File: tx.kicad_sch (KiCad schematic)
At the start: 48 parts, among them J13 RFShield_Frame, J5 SWH, J7 SMA, T2 RF_BALUN, U12 MAX2831, U13 TXIF_BALUN, U16 DPDT

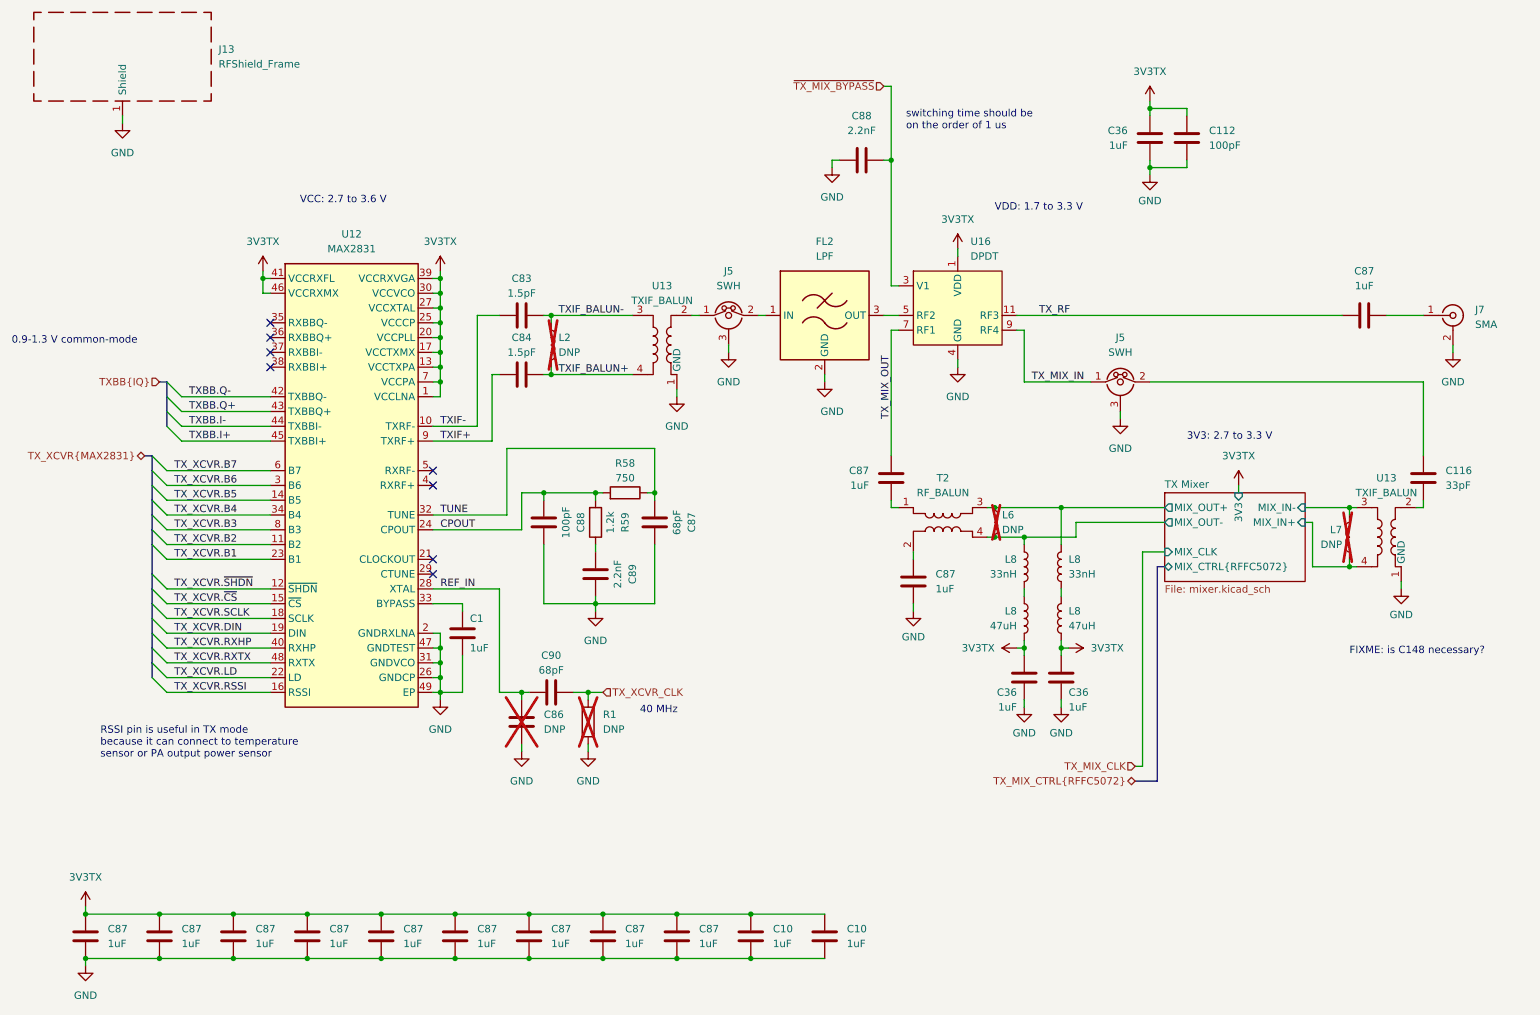
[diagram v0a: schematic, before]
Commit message: Replace open drain clock inverters with push-pull
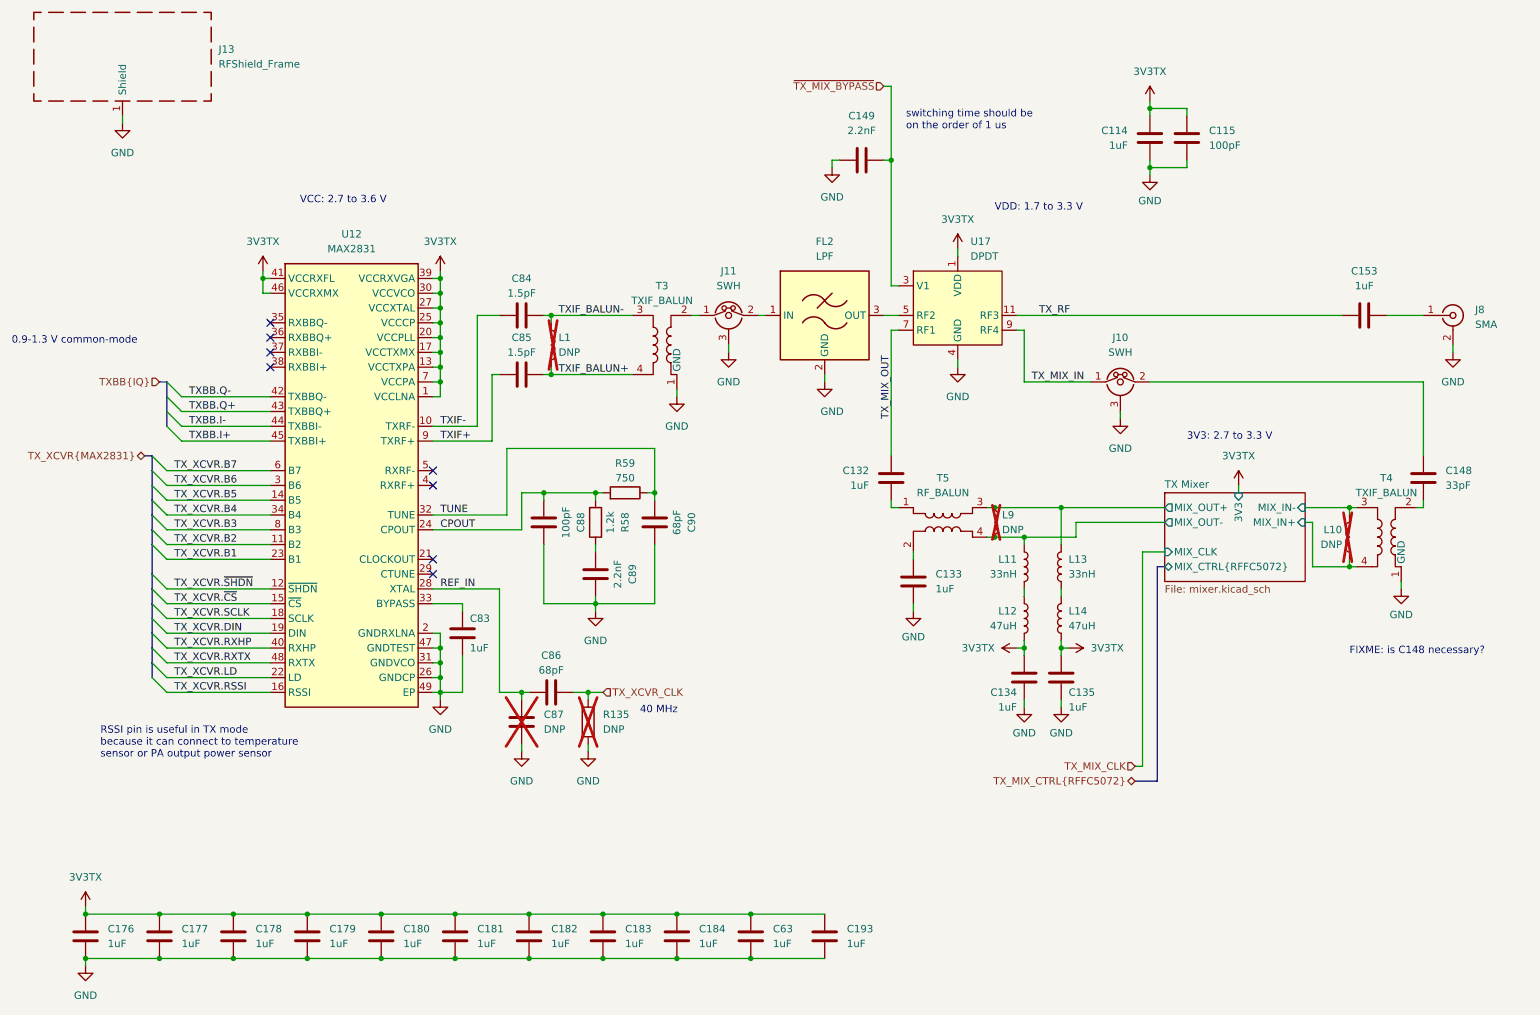
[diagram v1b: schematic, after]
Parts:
- renumbered C36 to C114, C112 to C115, C87 to C132, C87 to C133, C36 to C134, C36 to C135, C116 to C148, C88 to C149, C87 to C153, C87 to C176, C87 to C177, C87 to C178, C87 to C179, C87 to C180, C87 to C181, C87 to C182, C87 to C183, C87 to C184, C10 to C193, C10 to C63, C1 to C83, C83 to C84, C84 to C85, C90 to C86, C86 to C87, C87 to C90, J5 to J10, J5 to J11, J7 to J8, L2 to L1, L7 to L10, L8 to L11, L8 to L12, L8 to L13, L8 to L14, L6 to L9, R1 to R135, R59 to R58, R58 to R59, U13 to T3, U13 to T4, T2 to T5, U16 to U17

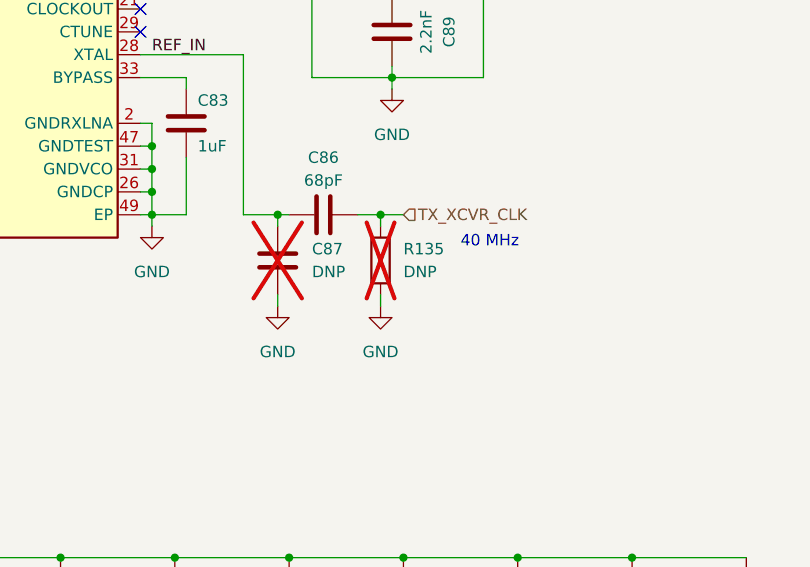
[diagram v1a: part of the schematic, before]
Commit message: Tune clock passives
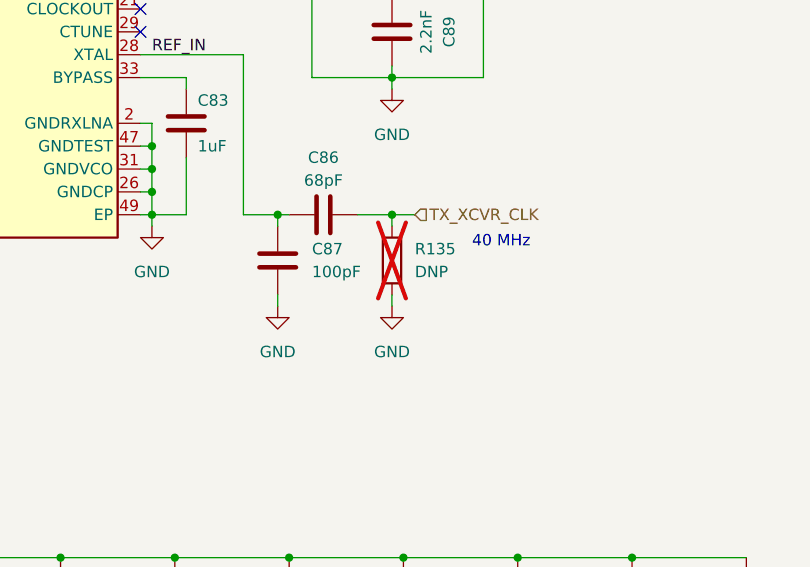
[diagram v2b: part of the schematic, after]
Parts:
- C87: value DNP -> 100pF; Manufacturer (none) -> Samsung; Part Number (none) -> CL03C101JA3NNNC; now fitted
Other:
- moved on the sheet: R135
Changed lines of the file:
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@@
   (junction (at 193.04 113.03) (diameter 0) (color 0 0 0 0)
   )
-  (junction (at 118.11 139.7) (diameter 0) (color 0 0 0 0)
+  (junction (at 119.38 139.7) (diameter 0) (color 0 0 0 0)
   )
   (junction (at 82.55 177.8) (diameter 0) (color 0 0 0 0)
@@
     (stroke (width 0) (type default))
   )
-  (wire (pts (xy 118.11 148.59) (xy 118.11 149.86))
+  (wire (pts (xy 119.38 148.59) (xy 119.38 149.86))
     (stroke (width 0) (type default))
   )
@@
     (stroke (width 0) (type default))
   )
-  (wire (pts (xy 118.11 139.7) (xy 120.65 139.7))
+  (wire (pts (xy 119.38 139.7) (xy 121.92 139.7))
     (stroke (width 0) (type default))
   )
@@
     (stroke (width 0) (type default))
   )
-  (wire (pts (xy 118.11 139.7) (xy 118.11 140.97))
+  (wire (pts (xy 119.38 139.7) (xy 119.38 140.97))
     (stroke (width 0) (type default))
   )
@@
     (stroke (width 0) (type default))
   )
-  (wire (pts (xy 115.57 139.7) (xy 118.11 139.7))
+  (wire (pts (xy 115.57 139.7) (xy 119.38 139.7))
     (stroke (width 0) (type default))
   )
@@
     (stroke (width 0) (type default))
   )
-  (text "40 MHz" (at 127 143.51 0)
+  (text "40 MHz" (at 128.27 143.51 0)
     (effects (font (size 1.27 1.27)) (justify left bottom))
   )
@@
     (effects (font (size 1.27 1.27)) (justify right))
   )
-  (hierarchical_label "TX_XCVR_CLK" (shape input) (at 120.65 139.7 0) (fields_autoplaced)
+  (hierarchical_label "TX_XCVR_CLK" (shape input) (at 121.92 139.7 0) (fields_autoplaced)
     (effects (font (size 1.27 1.27)) (justify left))
   )
@@
     )
   )
-  (symbol (lib_id "Device:R") (at 118.11 144.78 0) (unit 1)
+  (symbol (lib_id "Device:R") (at 119.38 144.78 0) (unit 1)
     (in_bom yes) (on_board yes) (dnp yes) (fields_autoplaced)
-    (property "Reference" "R135" (at 120.65 143.51 0)
+    (property "Reference" "R135" (at 121.92 143.51 0)
       (effects (font (size 1.27 1.27)) (justify left))
     )
-    (property "Value" "DNP" (at 120.65 146.05 0)
+    (property "Value" "DNP" (at 121.92 146.05 0)
       (effects (font (size 1.27 1.27)) (justify left))
     )
-    (property "Footprint" "Resistor_SMD:R_0402_1005Metric" (at 116.332 144.78 90)
-      (effects (font (size 1.27 1.27)) hide)
-    )
-    (property "Datasheet" "~" (at 118.11 144.78 0)
-      (effects (font (size 1.27 1.27)) hide)
-    )
-    (property "Part Number" "" (at 118.11 144.78 0)
-      (effects (font (size 1.27 1.27)) hide)
-    )
-    (property "Substitution" "" (at 118.11 144.78 0)
-      (effects (font (size 1.27 1.27)) hide)
-    )
-    (property "Description" "" (at 118.11 144.78 0)
-      (effects (font (size 1.27 1.27)) hide)
-    )
-    (property "Manufacturer" "" (at 118.11 144.78 0)
+    (property "Footprint" "Resistor_SMD:R_0402_1005Metric" (at 117.602 144.78 90)
+      (effects (font (size 1.27 1.27)) hide)
+    )
+    (property "Datasheet" "~" (at 119.38 144.78 0)
+      (effects (font (size 1.27 1.27)) hide)
+    )
+    (property "Part Number" "" (at 119.38 144.78 0)
+      (effects (font (size 1.27 1.27)) hide)
+    )
+    (property "Substitution" "" (at 119.38 144.78 0)
+      (effects (font (size 1.27 1.27)) hide)
+    )
+    (property "Description" "" (at 119.38 144.78 0)
+      (effects (font (size 1.27 1.27)) hide)
+    )
+    (property "Manufacturer" "" (at 119.38 144.78 0)
       (effects (font (size 1.27 1.27)) hide)
     )
@@
   )
   (symbol (lib_id "Device:C") (at 106.68 144.78 0) (unit 1)
-    (in_bom yes) (on_board yes) (dnp yes) (fields_autoplaced)
+    (in_bom yes) (on_board yes) (dnp no) (fields_autoplaced)
     (property "Reference" "C87" (at 110.49 143.51 0)
       (effects (font (size 1.27 1.27)) (justify left))
     )
-    (property "Value" "DNP" (at 110.49 146.05 0)
+    (property "Value" "100pF" (at 110.49 146.05 0)
       (effects (font (size 1.27 1.27)) (justify left))
     )
@@
       (effects (font (size 1.27 1.27)) hide)
     )
+    (property "Description" "CAP CER 100PF 25V C0G/NP0 0201" (at 106.68 144.78 0)
+      (effects (font (size 1.27 1.27)) hide)
+    )
+    (property "Manufacturer" "Samsung" (at 106.68 144.78 0)
+      (effects (font (size 1.27 1.27)) hide)
+    )
+    (property "Part Number" "CL03C101JA3NNNC" (at 106.68 144.78 0)
+      (effects (font (size 1.27 1.27)) hide)
+    )
     (pin "1")
     (pin "2")
@@
     )
   )
-  (symbol (lib_id "power:GND") (at 118.11 149.86 0) (unit 1)
+  (symbol (lib_id "power:GND") (at 119.38 149.86 0) (unit 1)
     (in_bom yes) (on_board yes) (dnp no) (fields_autoplaced)
-    (property "Reference" "#PWR0344" (at 118.11 156.21 0)
-      (effects (font (size 1.27 1.27)) hide)
-    )
-    (property "Value" "GND" (at 118.11 154.94 0)
-      (effects (font (size 1.27 1.27)))
-    )
-    (property "Footprint" "" (at 118.11 149.86 0)
-      (effects (font (size 1.27 1.27)) hide)
-    )
-    (property "Datasheet" "" (at 118.11 149.86 0)
-      (effects (font (size 1.27 1.27)) hide)
-    )
+    (property "Reference" "#PWR0344" (at 119.38 156.21 0)
+      (effects (font (size 1.27 1.27)) hide)
+    )
+    (property "Value" "GND" (at 119.38 154.94 0)
+      (effects (font (size 1.27 1.27)))
+    )
+    (property "Footprint" "" (at 119.38 149.86 0)
+      (effects (font (size 1.27 1.27)) hide)
+    )
+    (property "Datasheet" "" (at 119.38 149.86 0)
+      (effects (font (size 1.27 1.27)) hide)
+    )
